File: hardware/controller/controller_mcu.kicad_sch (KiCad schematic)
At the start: 15 parts, among them J9 UART, SW1 RESET, SW2 BOOT, U3 ESP32-S3-WROOM-1U-N8

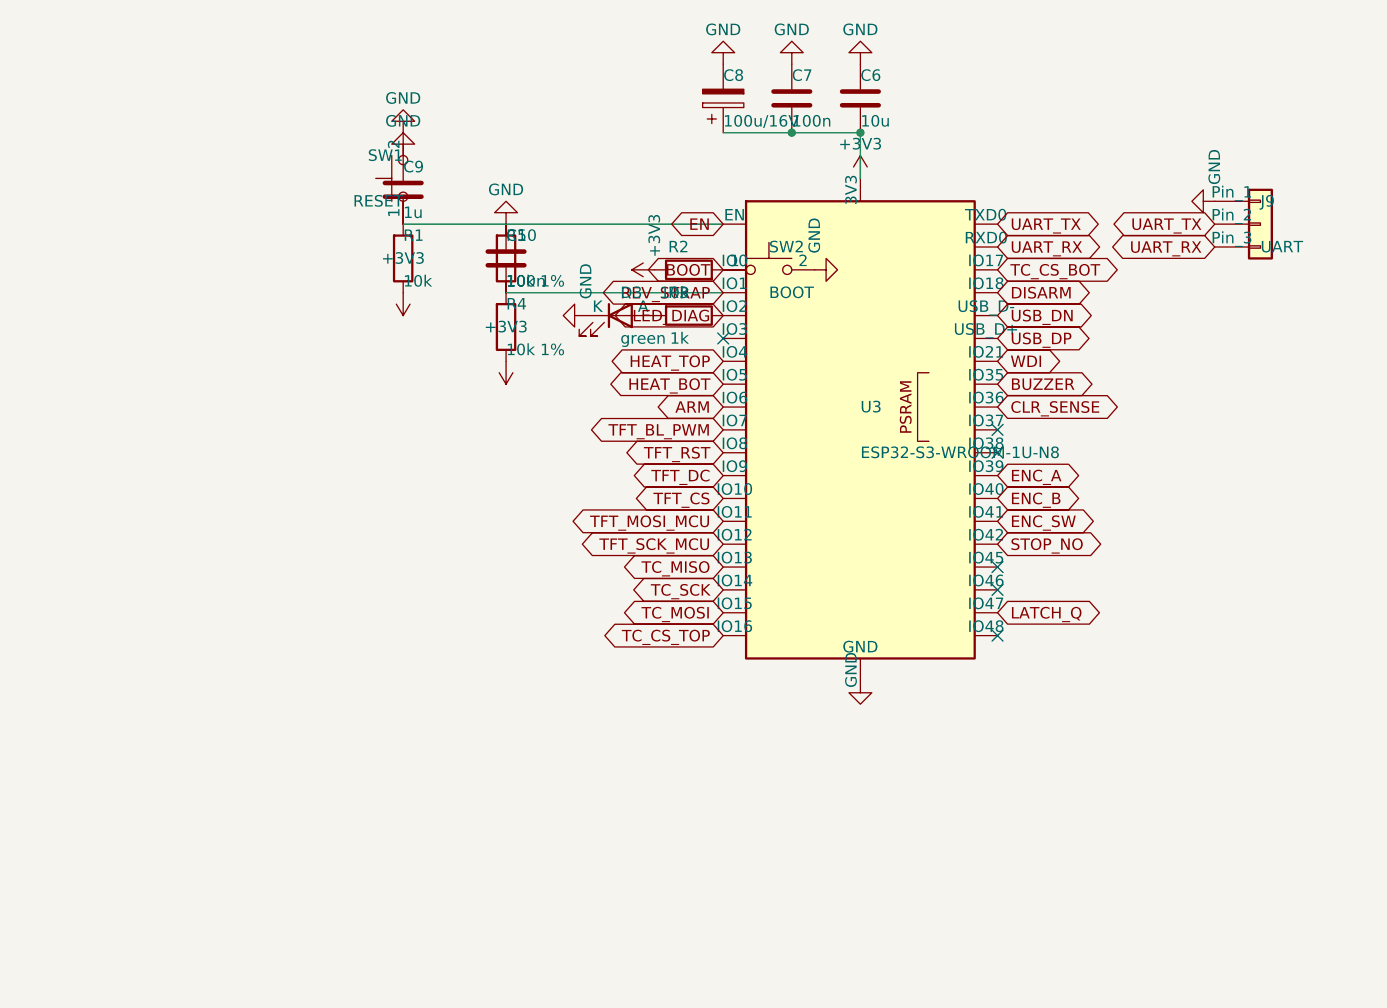
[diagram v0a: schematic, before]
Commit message: feat(hardware): MAX31856 input filter per datasheet, sheet cleanup in progress
- Input filter per MAX31856 "Typical Application Circuit": C14/C17 100 nF
  differential, new C27-C30 10 nF from T+/T- to GND; reference netlist re-exported
- Datasheet checks: BIAS to T- confirmed, FAULT is push-pull (diodes to CLR needed)
- check_schematic.py: sheet format check (raw newline in strings breaks KiCad)
- import_netlist.py: relinks by reference when a symbol gets a new UUID (U7 case)
- Sheets partly rearranged in KiCad by the user (connectivity unchanged, 0 errors)
- MAX31856 order number and price, docs/Component-Specs ignored

Co-Authored-By: Claude Opus 5.5 <noreply@anthropic.com>
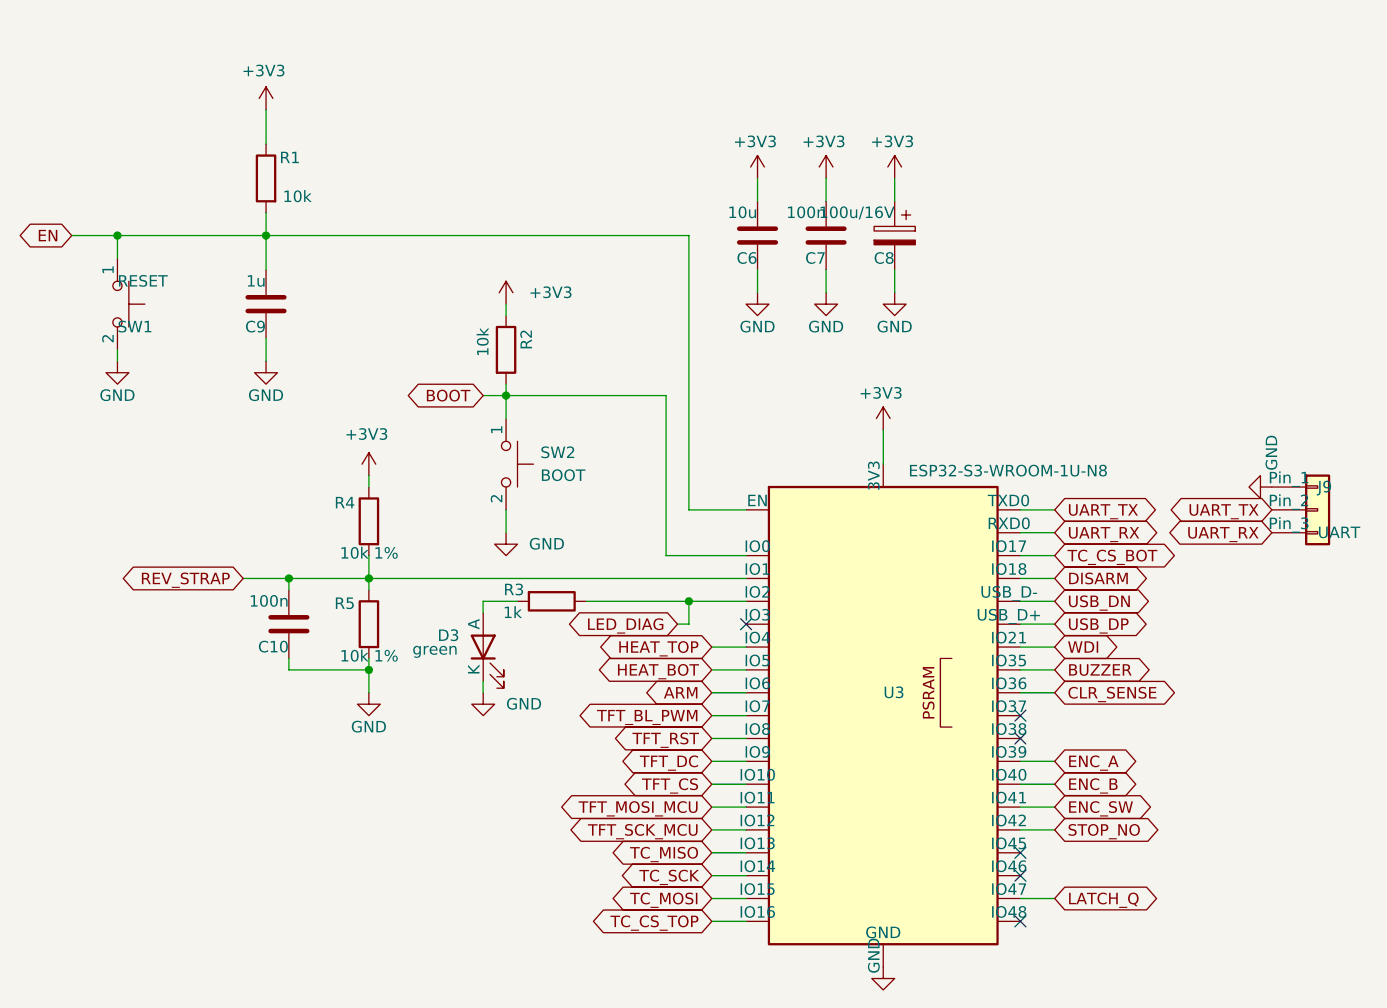
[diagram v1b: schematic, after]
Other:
- moved on the sheet: C10, C6, C7, C8, C9, D3, J9, R1, R2, R3, R4, R5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
